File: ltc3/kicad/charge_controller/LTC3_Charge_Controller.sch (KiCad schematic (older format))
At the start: 119 parts, among them P1 MicroFit header, P2 MicroFit header, P3 JST XH header, P4 MicroFit header, P5 JST XH header, P6 JST XH header, Q1 ZVN4525E6, Q2 BSC028N06NS, Q3 BSC028N06NS, Q4 BSC028N06NS, Q5 BSC028N06NS, Q6 ZVP3310F, Q7 MMBT5550L, U1 PI2127, U2 PI2127, U3 LT8490, U4 LTC2990

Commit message: LTC3: Corrected charge controller shunt resistor BOM data.
Really done this time, for reals.
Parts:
- P6: Spec - -> (none)
- R19, R3, R4, R40: Mfg_Description (none) -> 1% 1/8W
- R20, R38: footprint Resistors_SMD:R_2512 -> Resistors_SMD:R_1206; Mfg_Name Bourns -> Vishay; Mfg_PN CST0612-FC-R0015E -> WSLP1206R0100FEA
- R31: footprint Resistors_SMD:R_1210_HandSoldering -> Resistors_SMD:R_1206; Mfg_Description 1% 1W -> 1% 1/4W; Mfg_Name Bourns -> Vishay; Mfg_PN CST0612-FC-R0015E -> WSL12065L000FEA
- R42: footprint Resistors_SMD:R_2512 -> Resistors_SMD:R_1206; Mfg_Name Yageo -> Samsung; Mfg_PN RL2512FK-070R1L -> RUW3216FR100CS

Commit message: LTC3: One last correction to charge controller BOM.
And I'm serious this time.
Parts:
- R34: Mfg_PN storm eye -> RC0603JR-070RL

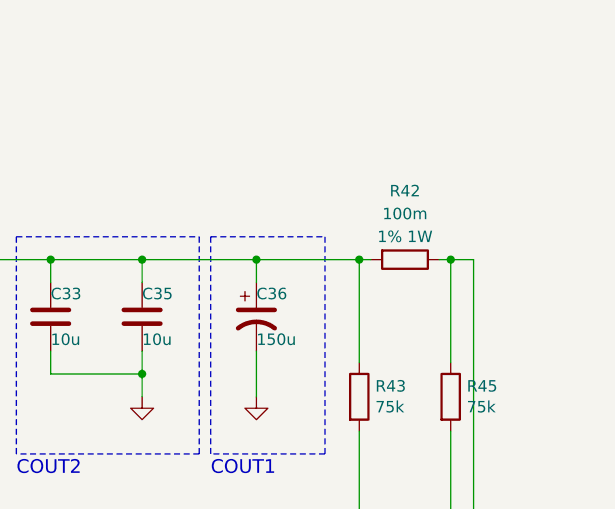
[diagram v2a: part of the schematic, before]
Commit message: LTC3: Corrected LTC2990 shunt resistor spec, etc.
I was only kidding about being finished.
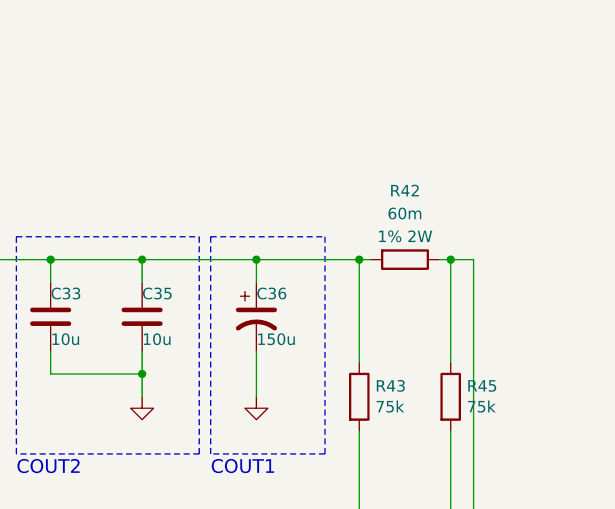
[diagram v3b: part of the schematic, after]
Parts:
- R42: value 100m -> 60m; footprint Resistors_SMD:R_1206 -> Resistors_SMD:R_2512; Mfg_Description 1% 1W -> 1% 2W; Mfg_Name Samsung -> Yageo; Mfg_PN RUW3216FR100CS -> PE2512FKE7W0R06L; Spec 1% 1W -> 1% 2W

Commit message: LTC3: Minor modification to Charge Controller DC input connectors.
Combined P1 (PV_IN) and P2 (LAB_IN) connectors into a single 2x2
(4-pos) MicroFit connector (DC_IN).
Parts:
- removed P1: MicroFit header, Connectors_Molex:Molex_Microfit3_Header_02x01_Straight_43045-0228, symbol CONN_01X02
- removed P2: MicroFit header, Connectors_Molex:Molex_Microfit3_Header_02x02_Straight_43045-0428, symbol CONN_01X02
- added P1: MicroFit header, Connectors_Molex:Molex_Microfit3_Header_02x02_Straight_43045-0428, symbol CONN_01X04
- C1: value 0.33u -> 0.33μ
- C10, C8: value 0.01u -> 0.01μ
- C11, C12, C14, C20, C21, C9: value 2.2u -> 2.2μ
- C2, C4, C5: value 33u -> 33μ
- C22, C23: value 0.001u -> 0.001μ
- C24, C28, C29, C6, C7: value 4.7u -> 4.7μ
- C25, C30: value 1u -> 1μ
- C26, C3, C31, C34, C37: value 0.1u -> 0.1μ
- C27: value 0.18u -> 0.18μ
- C33, C35: value 10u -> 10μ
- C36: value 150u -> 150μ
- P3: value JST XH header -> XH header; Mfg_Description (none) -> 2-pos vertical header; Note - -> to thermistor
- P4: footprint Connectors_Molex:Molex_Microfit3_Header_02x02_Straight_43045-0428 -> Connectors_Molex:Molex_Microfit3_Header_02x01_Straight_43045-0228; Mfg_Description (none) -> 2-pos vertical header; Note - -> to cell protection
- P5: value JST XH header -> XH header; Mfg_Description (none) -> 2-pos vertical header; Note To LTC -> to LTC
- P6: value JST XH header -> XH header; Mfg_Description (none) -> 4-pos vertical header; Note To LTC -> to LTC
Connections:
- net GND: now also P1.2 (P2), P1.3 (P3)
- net PV_IN: now reaches U1.12 (S), U1.13 (S), U1.14 (S), U1.15 (SP), U1.16 (S), W3.1
- net PV_IN: now also P1.4 (P4)
- net LAB_IN: now reaches F1.1
- net LAB_IN: now also P1.1 (P1)
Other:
- note removed: "thermistor"
- moved on the sheet: W3

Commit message: LTC3: Minor changes to Charge Controller BOM.
Nothing that impacts PCB layout.
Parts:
- P1, P6: Mfg_Description 4-pos vertical header -> 4 pos vertical header
- P3, P4, P5: Mfg_Description 2-pos vertical header -> 2 pos vertical header

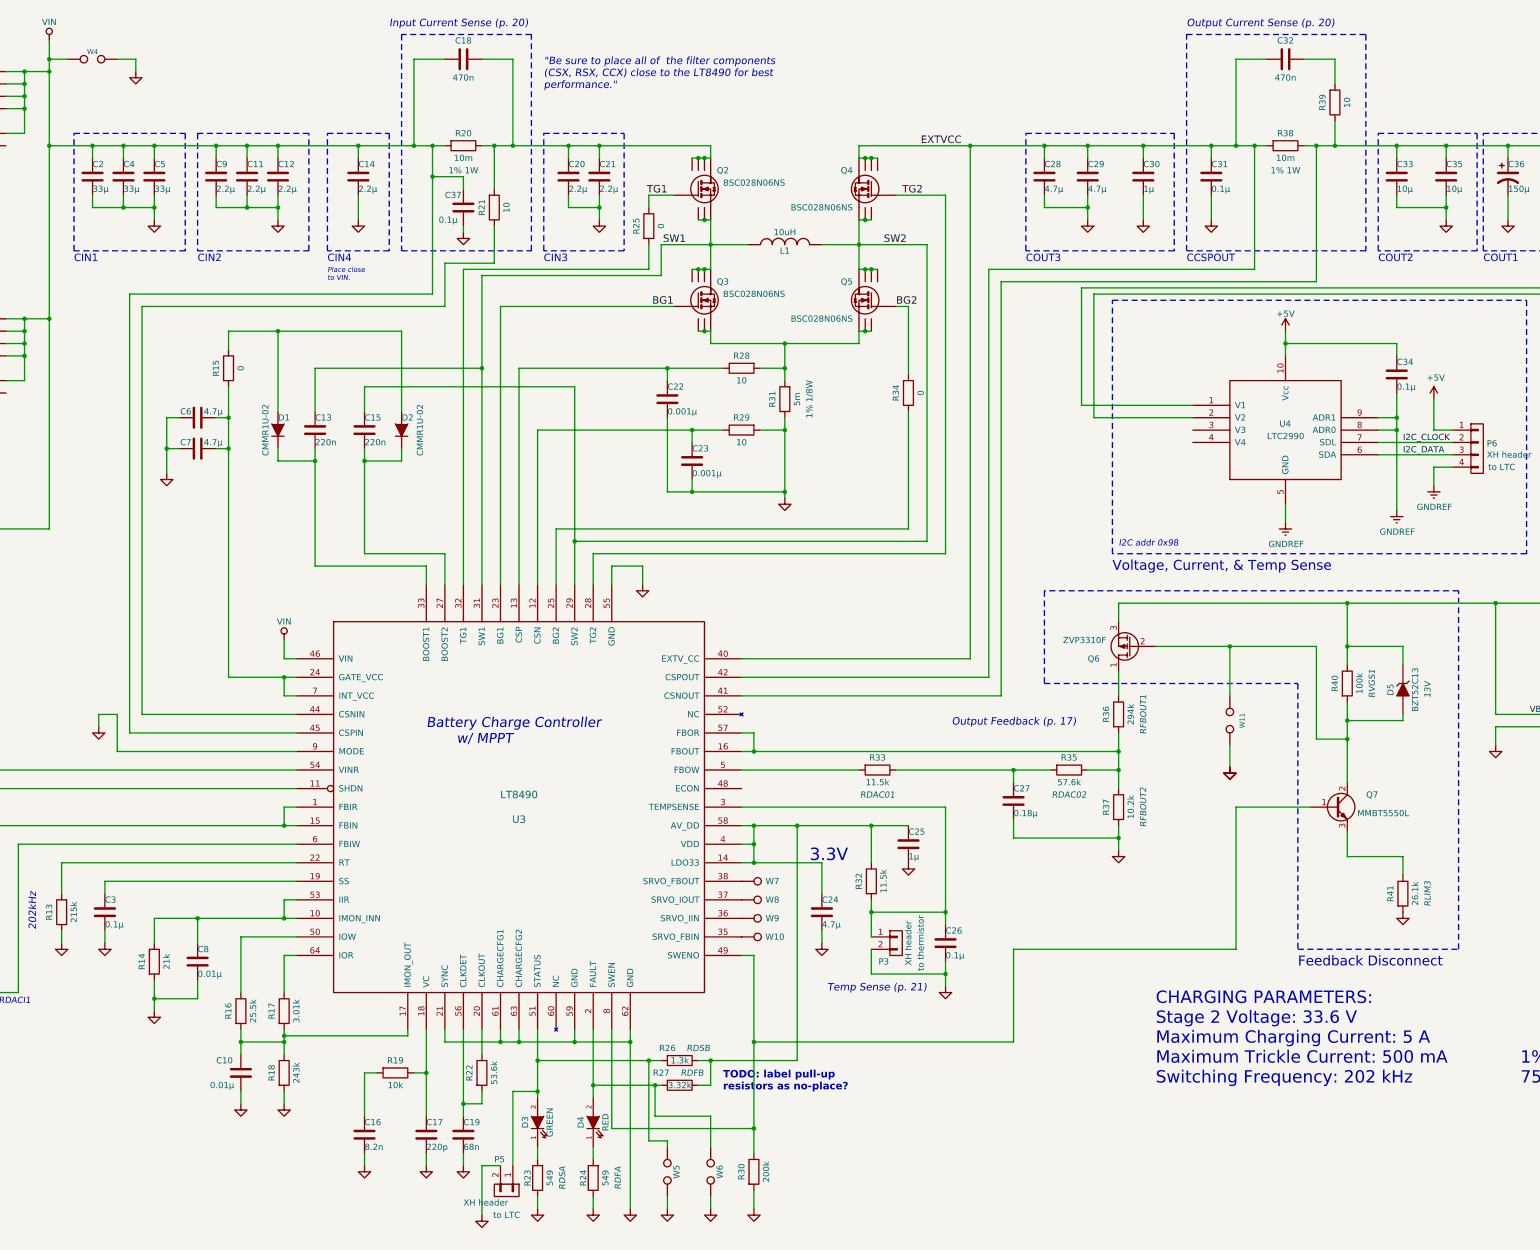
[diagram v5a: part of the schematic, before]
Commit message: LTC3: Layout Review Notes & Small Changes
Added some changes from the layout review today.
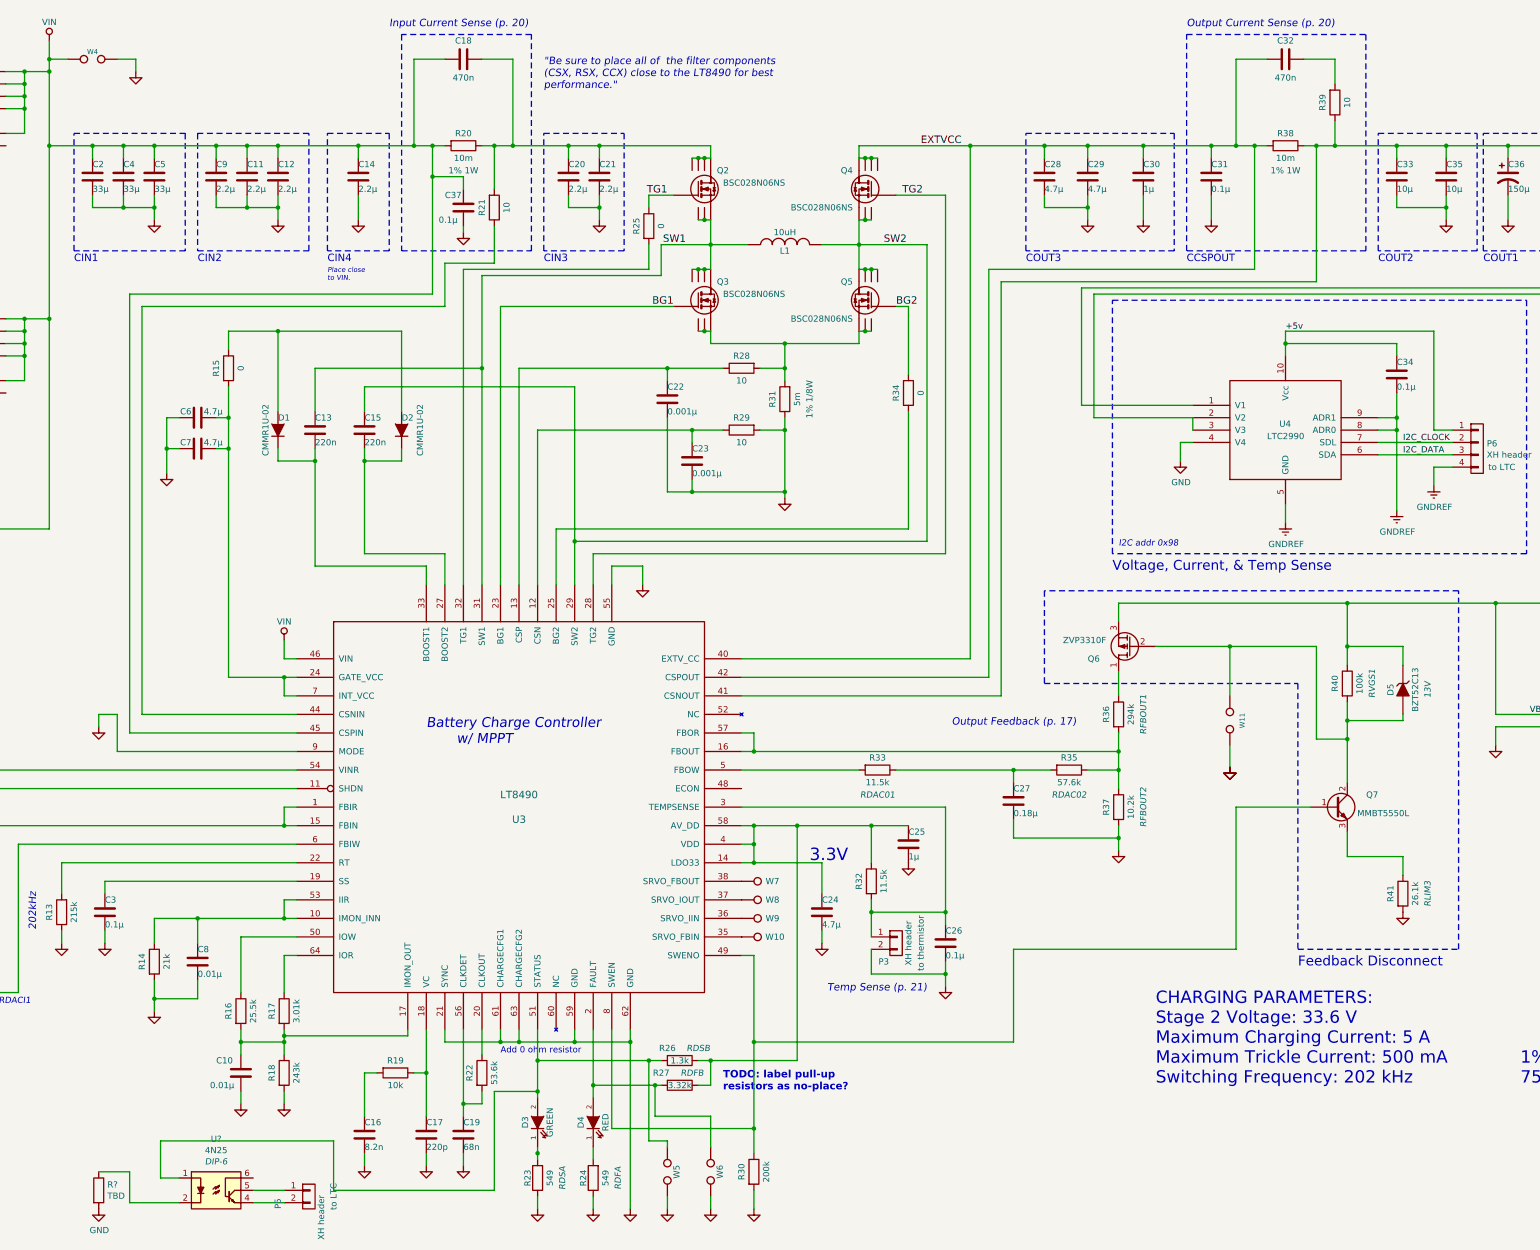
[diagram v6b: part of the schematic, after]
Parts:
- added R?: TBD, symbol R
- added U?: 4N25, DIP-6, symbol 4N25
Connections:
- net GND: now also U4.4 (V4), R?.2; no longer P5.2 (P2)
- net at D3.2 (A), R26.2, U3.51 (STATUS)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: now also U?.1; no longer P5.1 (P1)
- net at R45.2, R46.1, U4.2 (V2): now also U4.3 (V3)
- net +5V renamed +5v
- new net: P5.1 (P1), U?.5
- new net: P5.2 (P2), U?.4
- new net: R?.1, U?.2
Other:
- note added: "Add 0 ohm resistor"
- moved on the sheet: P5
